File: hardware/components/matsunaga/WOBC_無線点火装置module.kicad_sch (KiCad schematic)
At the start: 22 parts, among them Q1 NPN, Q2 BS250, Q3 BS170, SW1 SW_DPDT_x2

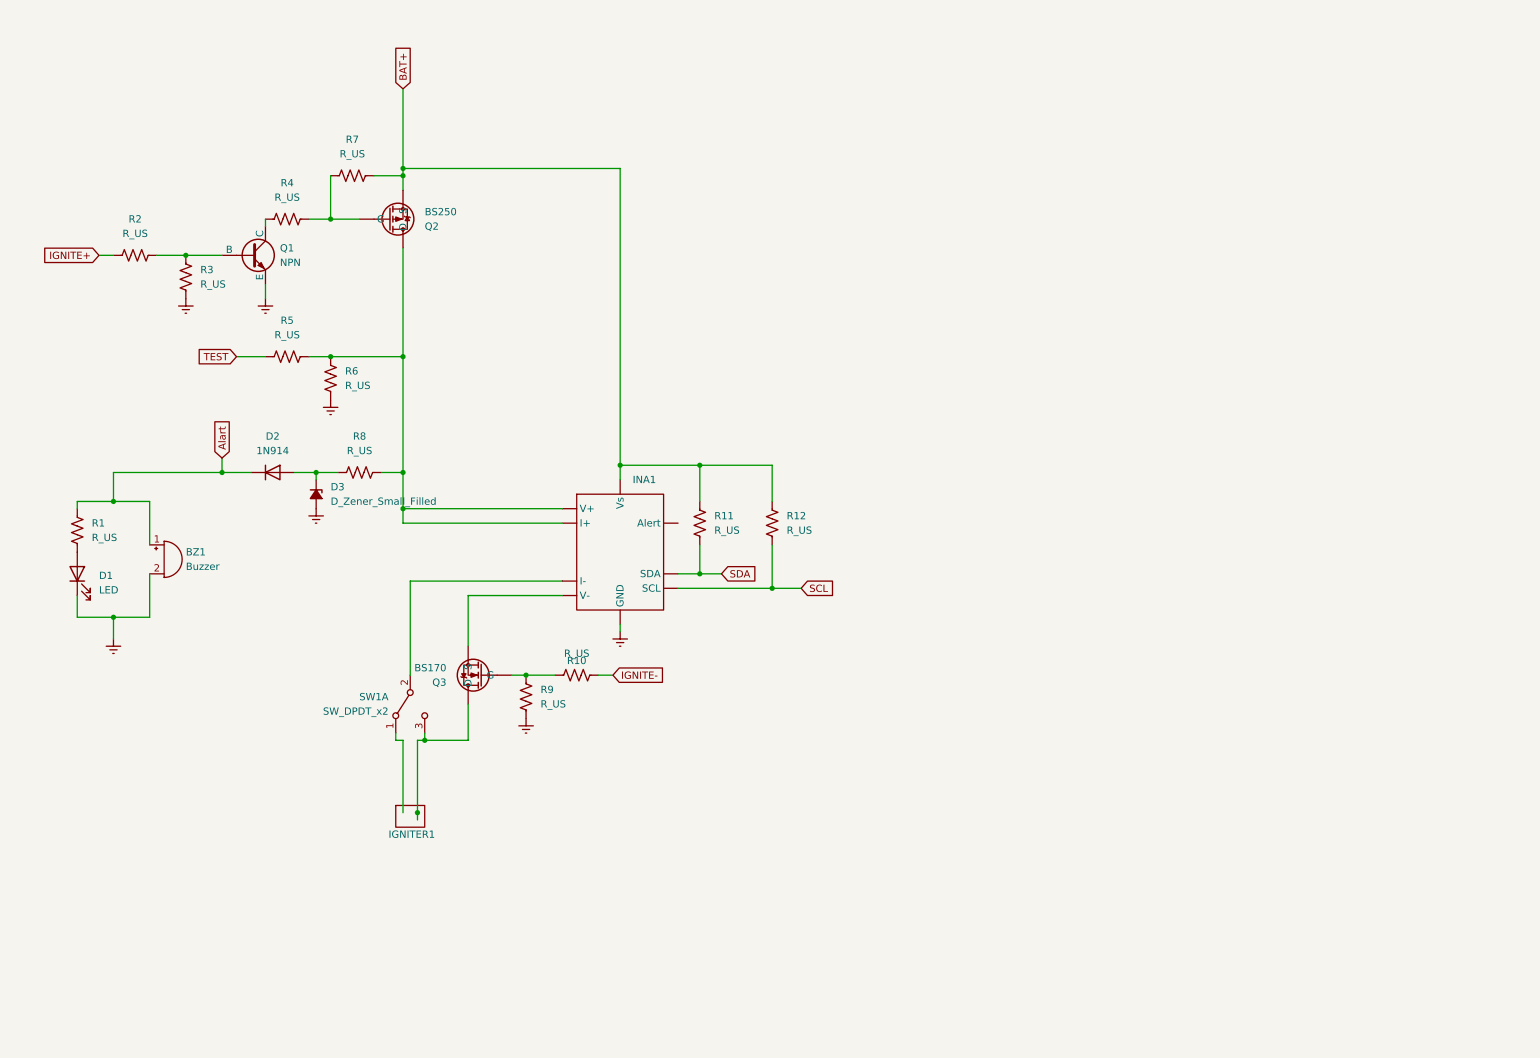
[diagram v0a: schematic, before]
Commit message: 抵抗値一部追加
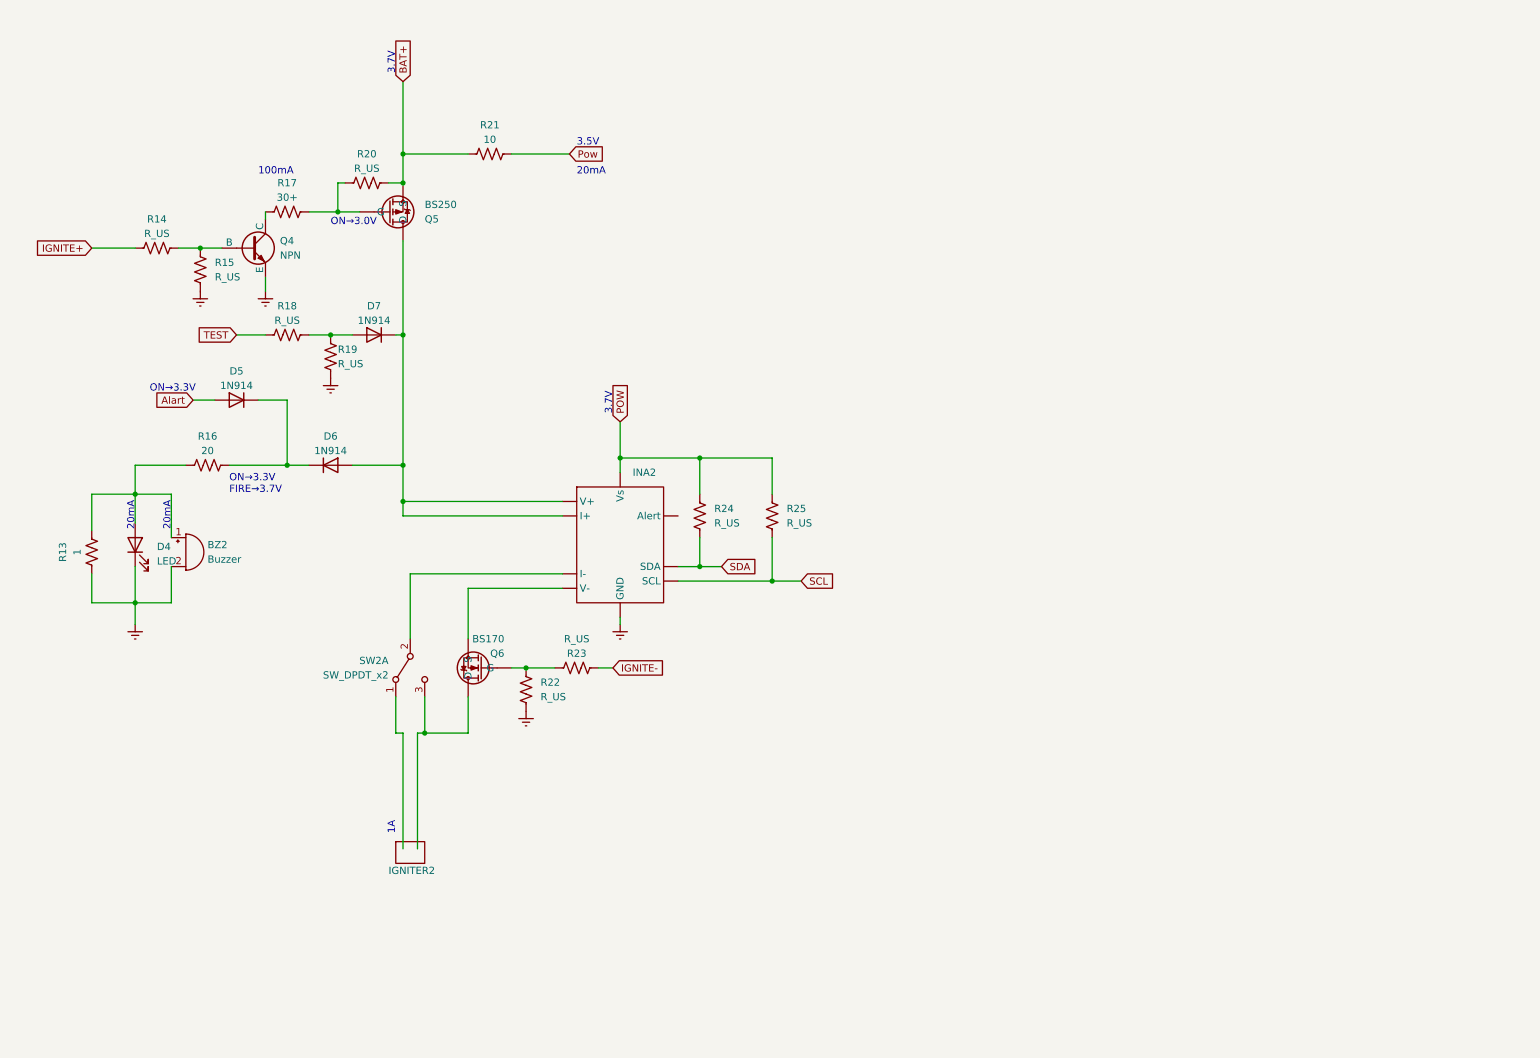
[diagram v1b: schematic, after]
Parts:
- removed BZ1: Buzzer, symbol Device:Buzzer
- removed D1: LED, symbol Device:LED
- removed D2: 1N914, Diode_THT:D_DO-35_SOD27_P7.62mm_Horizontal, symbol Diode:1N914
- removed D3: D_Zener_Small_Filled, symbol Device:D_Zener_Small_Filled
- removed IGNITER1: ~, symbol Modelrocket Igniter:SingleIgniter
- removed INA1: ~, symbol Currentmeter-Voltmeter:INA226_module
- removed Q1: NPN, symbol Simulation_SPICE:NPN
- removed Q2: BS250, Package_TO_SOT_THT:TO-92_Inline, symbol Transistor_FET:BS250
- removed Q3: BS170, Package_TO_SOT_THT:TO-92_Inline, symbol Transistor_FET:BS170
- removed R1, R10, R11, R12, R2, R3, R4, R5, R6, R7, R8, R9: R_US, symbol Device:R_US
- removed SW1: SW_DPDT_x2, symbol Switch:SW_DPDT_x2
- added BZ2: Buzzer, symbol Device:Buzzer
- added D4: LED, symbol Device:LED
- added D5, D6, D7: 1N914, Diode_THT:D_DO-35_SOD27_P7.62mm_Horizontal, symbol Diode:1N914
- added IGNITER2: ~, symbol Modelrocket Igniter:SingleIgniter
- added INA2: ~, symbol Currentmeter-Voltmeter:INA226_module
- added Q4: NPN, symbol Simulation_SPICE:NPN
- added Q5: BS250, Package_TO_SOT_THT:TO-92_Inline, symbol Transistor_FET:BS250
- added Q6: BS170, Package_TO_SOT_THT:TO-92_Inline, symbol Transistor_FET:BS170
- added R13: 1, symbol Device:R_US
- added R14, R15, R18, R19, R20, R22, R23, R24, R25: R_US, symbol Device:R_US
- added R16: 20, symbol Device:R_US
- added R17: 30+, symbol Device:R_US
- added R21: 10, symbol Device:R_US
- added SW2: SW_DPDT_x2, symbol Switch:SW_DPDT_x2
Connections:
- net Alart: now also D5.2 (A)
- net BAT+: now also Q5.3 (S), R20.1, R21.2
- net Earth: now also BZ2.2 (+), D4.1 (K), INA2. (Vs), Q4.3 (E), R13.1, R15.1, R19.2, R22.1
- net IGNITE+: now also R14.2
- net IGNITE-: now also R23.1
- net SCL: now also INA2. (Vs), R25.2
- net SDA: now also INA2. (Vs), R24.2
- net TEST: now also R18.2
- new net: IGNITER2., SW2.1 (A)
- new net: INA2. (Vs), SW2.2 (B)
- new net: IGNITER2., Q6.1 (D), SW2.3 (C)
- new net: D7.2 (A), R18.1, R19.1
- new net: Q6.2 (G), R22.2, R23.2
- new net: BZ2.1 (-), D4.2 (A), R13.2, R16.1
- new net: INA2. (Vs), Q6.3 (S)
- new net: Q4.2 (B), R14.1, R15.2
- new net: D6.2 (A), D7.1 (K), INA2. (Vs), Q5.1 (D)
- new net: D5.1 (K), D6.1 (K), R16.2
- new net: Q5.2 (G), R17.1, R20.2
- new net: Q4.1 (C), R17.2
- new net POW: INA2. (Vs), R24.1, R25.1
- new net Pow: R21.1
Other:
- note added: "100mA"
- note added: "1A"
- note added: "20mA"
- note added: "3.5V"
- note added: "3.7V"
- note added: "ON→3.0V"
- note added: "ON→3.3V"
- note added: "ON→3.3V FIRE→3.7V"

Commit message: New Changes 20240111
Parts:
- removed BZ2: Buzzer, symbol Device:Buzzer
- removed D4: LED, symbol Device:LED
- removed D5, D6, D7: 1N914, Diode_THT:D_DO-35_SOD27_P7.62mm_Horizontal, symbol Diode:1N914
- removed IGNITER2: ~, symbol Modelrocket Igniter:SingleIgniter
- removed INA2: ~, symbol Currentmeter-Voltmeter:INA226_module
- removed Q4: NPN, symbol Simulation_SPICE:NPN
- removed Q5: BS250, Package_TO_SOT_THT:TO-92_Inline, symbol Transistor_FET:BS250
- removed Q6: BS170, Package_TO_SOT_THT:TO-92_Inline, symbol Transistor_FET:BS170
- removed R13: 1, symbol Device:R_US
- removed R16: 20, symbol Device:R_US
- removed R17: 30+, symbol Device:R_US
- removed R18, R19, R20, R22, R23, R24, R25: R_US, symbol Device:R_US
- removed R21: 10, symbol Device:R_US
- removed SW2: SW_DPDT_x2, symbol Switch:SW_DPDT_x2
- added BZ1: Buzzer, symbol Device:Buzzer
- added D1: LED, symbol Device:LED
- added D2, D3: 1N914, Diode_THT:D_DO-35_SOD27_P7.62mm_Horizontal, symbol Diode:1N914
- added FLIGHTPIN1, IGNITER1: ~, symbol Modelrocket Igniter:SingleIgniter
- added INA1: ~, symbol Currentmeter-Voltmeter:INA226_module
- added Q1: NPN, symbol Simulation_SPICE:NPN
- added Q2: 2SJ496, Package_TO_SOT_THT:TO-92_Inline, symbol Transistor_FET:BS250
- added Q3: BS170, Package_TO_SOT_THT:TO-92_Inline, symbol Transistor_FET:BS170
- added R1, R3, R5: 20, symbol Device:R_US
- added R10, R11: R_US, symbol Device:R_US
- added R2, R4, R8, R9: 100, symbol Device:R_US
- added R6: 510, symbol Device:R_US
- added R7: 1000, symbol Device:R_US
- added RP1: ~, symbol miconboard:Seeed_Xiao_RP2040
- added SW1: SW_DPDT_x2, symbol Switch:SW_DPDT_x2
- added TWE1: ~, symbol miconboard:TWELITE_UART
- R14, R15: value R_US -> 10000
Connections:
- net Alart: now also D2.2 (A)
- net BAT+: now also R15.1, INA1. (Vs), Q2.3 (S), R10.1, R11.1, R7.1, RP1. (GND)
- net Earth: now also BZ1.2 (+), D1.1 (K), INA1. (Vs), Q1.3 (E), R3.2, R4.1, R8.1; no longer R15.1
- net IGNITE+: now also R2.2, RP1. (GND); no longer R14.2
- net IGNITE-: now also R9.1, RP1. (GND)
- net SCL: now also INA1. (Vs), R11.2, RP1. (GND)
- net SDA: now also INA1. (Vs), R10.2, RP1. (GND)
- net TEST: now also RP1. (GND)
- net at R15.2: now also R14.2, TWE1. (VCC); no longer R14.1
- new net: FLIGHTPIN1., IGNITER1., SW1.1 (A)
- new net: INA1. (Vs), SW1.2 (B)
- new net: FLIGHTPIN1., IGNITER1., Q3.1 (D), SW1.3 (C)
- new net: Q3.2 (G), R8.2, R9.2
- new net: INA1. (Vs), Q3.3 (S)
- new net: D3.2 (A), INA1. (Vs), Q2.1 (D)
- new net: Q2.2 (G), R6.1, R7.2
- new net: Q1.1 (C), R6.2
- new net: BZ1.1 (-), D1.2 (A), R1.2
- new net: Q1.2 (B), R2.1, R4.2
- new net: D2.1 (K), D3.1 (K), R5.2
- new net: R1.1, R3.1, R5.1
- new net ALART: RP1. (GND)
- new net GND: R14.1, RP1. (GND), TWE1. (VCC)
- new net RX: RP1. (GND), TWE1. (VCC)
- new net TX: RP1. (GND), TWE1. (VCC)
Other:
- note added: "7.4V"
- note added: "ON→3V"
- note added: "↑ ON：2.5V→"
- note removed: "100mA"
- note removed: "3.5V"
- note removed: "ON→3.0V"

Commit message: Almost Complete
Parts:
- removed INA1: ~, symbol Currentmeter-Voltmeter:INA226_module
- removed Q2: 2SJ496, Package_TO_SOT_THT:TO-92_Inline, symbol Transistor_FET:BS250
- removed Q3: BS170, Package_TO_SOT_THT:TO-92_Inline, symbol Transistor_FET:BS170
- removed R15: 10000, symbol Device:R_US
- added BAT1: ~, 2pinconnector:3pin_connector, symbol Modelrocket Igniter:SingleIgniter
- added C1, C2: 10μF, Capacitor_SMD:C_1206_3216Metric_Pad1.33x1.80mm_HandSolder, symbol Device:C
- added C3, C4: 0.1u, Capacitor_SMD:C_1206_3216Metric_Pad1.33x1.80mm_HandSolder, symbol Device:C
- added CONNECTOR1, CONNECTOR2, CONNECTOR5, CONNECTOR6: ~, MyConnector:4pin_looseconnector, symbol MyConnector:4pin_looseconnector
- added CONNECTOR3, CONNECTOR4: ~, MyConnector:8pin_looseconnector, symbol MyConnector:8pin_looseconnector
- added Q2: NPN, transistors:npn, symbol Simulation_SPICE:NPN
- added Q3: 2SJ496, Package_TO_SOT_THT:TO-92_Inline, symbol Transistor_FET:BS250
- added Q4: BS170, Package_TO_SOT_THT:TO-92_Inline, symbol Transistor_FET:BS170
- added R12: 4.7, 2pinconnector:30mil, symbol Device:R_US
- added R13: 10000, 2pinconnector:30mil, symbol Device:R_US
- added U1: LM2940, Package_TO_SOT_SMD:TO-252-3_TabPin2, symbol Regulator_Linear:IFX27001TFV50
- added U2: INA226, Package_SO:VSSOP-10_3x3mm_P0.5mm, symbol Sensor_Energy:INA226
- BZ1: footprint (none) -> Buzzer_Beeper:Buzzer_15x7.5RM7.6
- D1: footprint (none) -> LEDS:SML-D12x1
- FLIGHTPIN1, IGNITER1: footprint (none) -> 2pinconnector:2pin_connector
- Q1: footprint (none) -> transistors:npn
- R1: value 20 -> 470; footprint (none) -> 2pinconnector:30mil
- R10: value R_US -> 10000; footprint (none) -> 2pinconnector:30mil
- R11: value R_US -> 4.7; footprint (none) -> 2pinconnector:30mil
- R14: value 10000 -> 0.002; footprint (none) -> 2pinconnector:0.002
- R2: value 100 -> 1000; footprint (none) -> 2pinconnector:1.05K
- R3: value 20 -> 1000; footprint (none) -> 2pinconnector:1.05K
- R4, R8: footprint (none) -> 2pinconnector:30mil
- R5: value 20 -> 510; footprint (none) -> 2pinconnector:1.05K
- R6: value 510 -> 10000; footprint (none) -> 2pinconnector:30mil
- R7: footprint (none) -> 2pinconnector:1.05K
- R9: value 100 -> 10000; footprint (none) -> 2pinconnector:30mil
- RP1: footprint (none) -> 2pinconnector:SeeedXiaoRP2040
- SW1: footprint (none) -> 2pinconnector:SW
- TWE1: footprint (none) -> 2pinconnector:TWELITE
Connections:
- net BAT+: now also SW1.2 (B), BAT1.1, C1.1, U1.3 (I); no longer R10.1, R11.1, R7.1, RP1. (GND)
- net Earth: now also BAT1.2, C1.2, C2.2, CONNECTOR1.1, Q2.3 (E), U1.1 (GND); no longer BZ1.2 (+), D1.1 (K), Q1.3 (E), R3.2, R4.1, R8.1
- net RX: now also RP1.7 (1), TWE1.2 (TXD); no longer RP1. (GND), TWE1. (VCC)
- net SCL: now also R9.1, RP1.9 (7), U2.5 (SCL); no longer R11.2, RP1. (GND)
- net SDA: now also R10.1, RP1.10 (6), U2.4 (SDA); no longer R10.2, RP1. (GND)
- net TEST: now also RP1.6 (2); no longer RP1. (GND)
- net TX: now also RP1.8 (0), TWE1.4 (RXD); no longer RP1. (GND), TWE1. (VCC)
- net IGNITE-2: now reaches R8.2
- net IGNITE-2: now also R7.1, CONNECTOR3.1; no longer R9.2
- net BAT3: now reaches D3.2 (A)
- net BAT3: now also R11.2, R14.1, CONNECTOR4.7
- net BAT1: now reaches R6.1
- net BAT1: now also SW1.1 (A), Q3.3 (S); no longer R7.2
- net at R6.2: now also R5.1, Q3.2 (G); no longer Q1.1 (C)
- net at D1.2 (A), R1.2: no longer BZ1.1 (-)
- net at D2.1 (K), D3.1 (K): now also BZ1.1 (-), R1.1; no longer R5.2
- net at R14.2: now also CONNECTOR5.1, R12.2; no longer TWE1. (VCC)
- removed net ALART: RP1. (GND)
- net Alart: no longer names the net of D2.2 (A)
- net Alart: now also Q1.3 (E)
- removed net GND: R14.1, RP1. (GND), TWE1. (VCC)
- net IGNITE+ renamed IGNITE+2
- net IGNITE+2: now also R4.1, CONNECTOR2.3; no longer RP1. (GND)
- removed net IGNITE-: R9.1, RP1. (GND)
- new net: Q2.1 (C), R5.2
- new net: CONNECTOR5.4, Q4.1 (D)
- new net: R8.1, RP1.13 (27)
- new net: R2.1, RP1.14 (26)
- new net: CONNECTOR6.1, FLIGHTPIN1.1, IGNITER1.1
- new net: CONNECTOR3.2, U2.8 (Vbus)
- new net: CONNECTOR3.3, U2.9 (Vin-)
- new net: Q1.2 (B), R3.1
- new net: R13.2, TWE1.6 (VCC)
- new net: C2.1, CONNECTOR1.4, U1.2 (Q)
- new net: C3.2, CONNECTOR4.2, R12.1
- new net: C3.1, CONNECTOR4.3, R11.1
- new net 3V3_2: CONNECTOR3.6, R13.1, RP1.3 (3V3)
- new net 3V3_3: CONNECTOR4.6, Q1.1 (C)
- new net ALART2: CONNECTOR3.5, RP1.12 (28)
- new net Alart3: CONNECTOR4.5, R3.2
- new net BAT1Z: CONNECTOR1.2, Q3.1 (D)
- new net BAT2: CONNECTOR2.2, CONNECTOR3.7, U2.10 (Vin+)
- new net GND2: C4.2, CONNECTOR2.1, CONNECTOR3.8, R4.2, R7.2, RP1.2 (GND), TWE1.1 (GND), U2.7 (GND)
- new net GND3: BZ1.2 (+), CONNECTOR4.8, D1.1 (K), Q4.3 (S)
- new net GND4: CONNECTOR6.4, FLIGHTPIN1.2, IGNITER1.2
- new net IGNITE+1: CONNECTOR1.3, Q2.2 (B)
- new net IGNITE-3: CONNECTOR4.1, Q4.2 (G)
- new net POW: C4.1, CONNECTOR2.4, R10.2, R9.2, RP1.1 (5V), U2.6 (VS)
- now unconnected: SW1.3 (C)
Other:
- note added: "+ -"
- note added: "BAT+"
- note added: "GND"
- note added: "POW"
- note added: "１枚目"
- note added: "２枚目"
- note added: "３枚目"
- note added: "４枚目"
- note removed: "3.7V"
- note removed: "7.4V"
- note removed: "ON→3.3V"
- note removed: "ON→3.3V FIRE→3.7V"
- note removed: "↑ ON：2.5V→"
